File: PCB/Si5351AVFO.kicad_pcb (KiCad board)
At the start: 4 copper layers, 100 x 65 mm, 121 parts, among them J1 USB_C_Receptacle, J2 SMA CLK0, J3 SMA CLK1, J4 SMA CLK2, J5 UPDI, SW1 EC11E18244A5, SW2 BAND, SW3 STEP, SW4 MENU, U1 LP2985-3.3, U2 Si5351A-B-GT, U3 CP2102N-A02-GQFN24, U4 ATtiny3226-SU, U5 LP2985-3.3, X1 25MHz TCXO

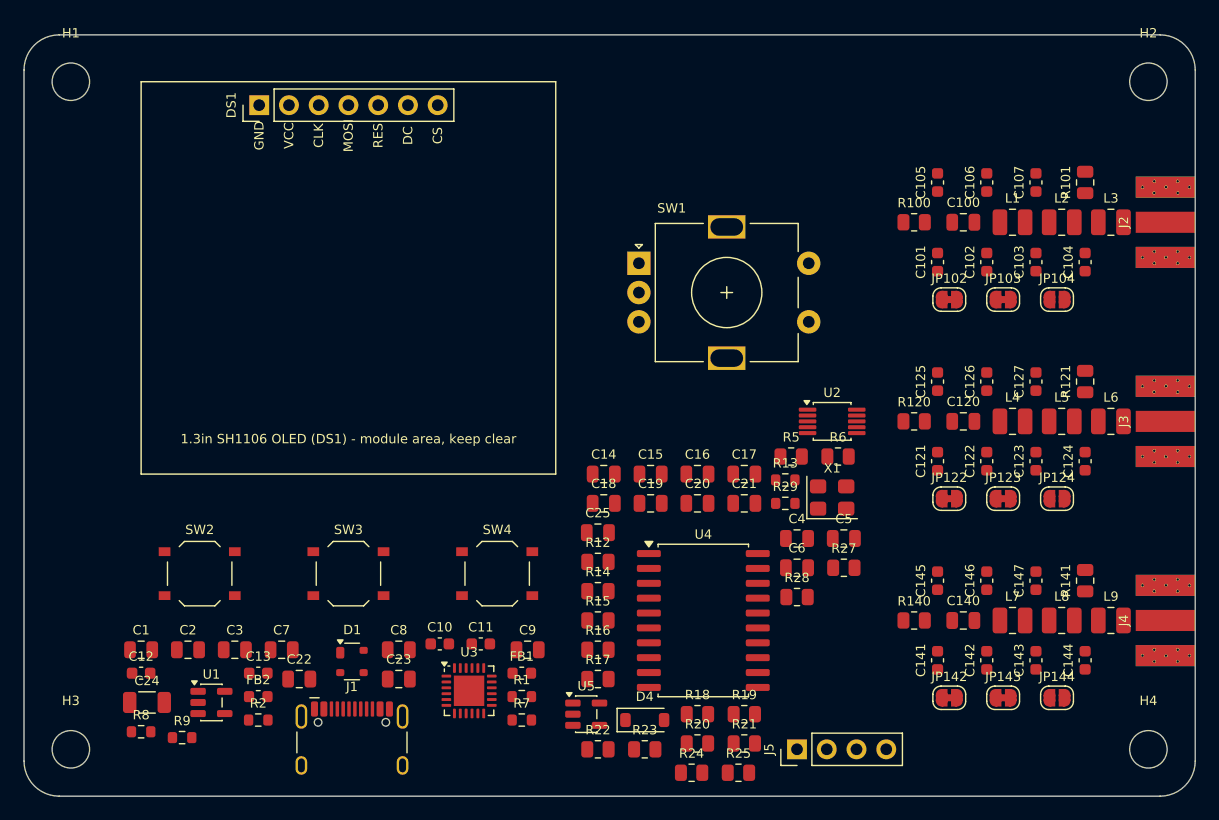
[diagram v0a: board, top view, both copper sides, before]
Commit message: Layout rev 2: USB-C + SMAs on top edge, RF block under SH1 fence, 11 mm tact switches, plated GND M3 holes, In1 cut under SMA centre pads, In1/In2 GND planes, Etherkit branding + Rev A on F.Cu; regen renders/outline/STEP
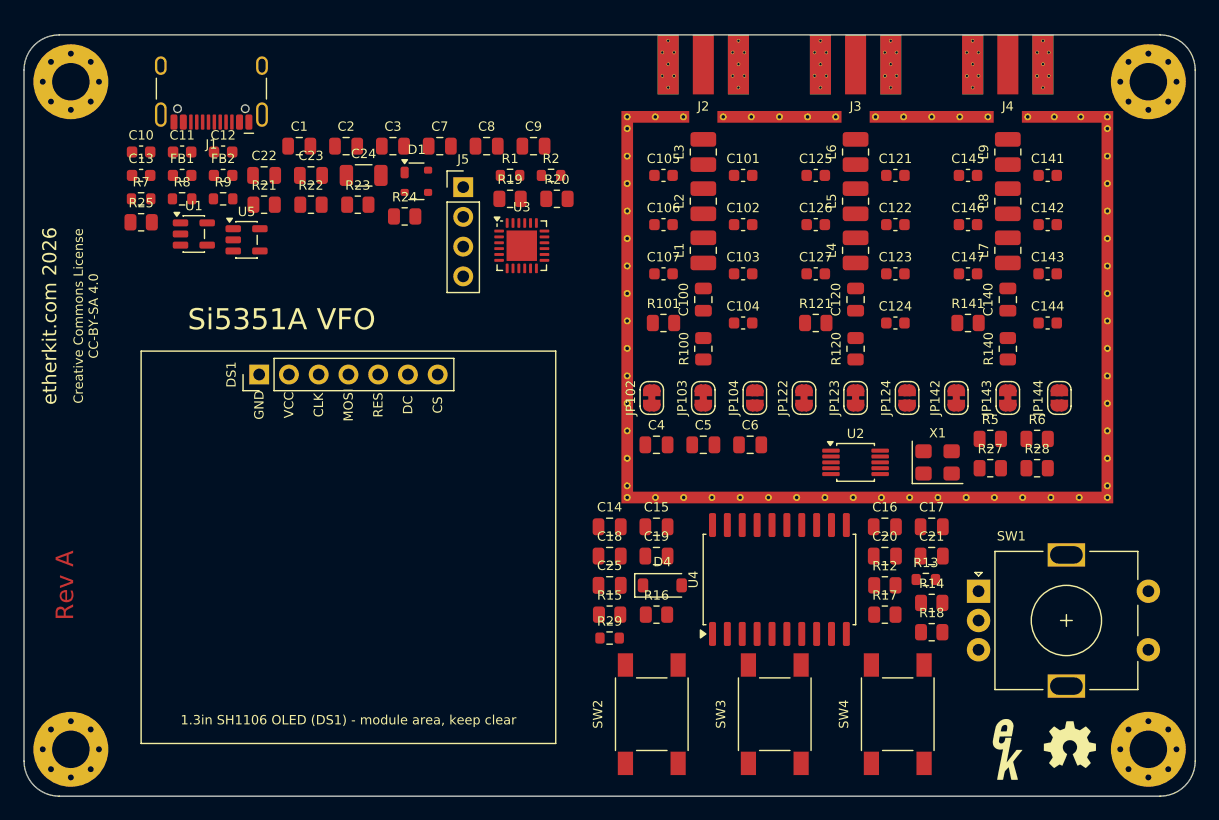
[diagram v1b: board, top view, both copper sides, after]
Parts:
- added LOGO1: Val**, EtherkitKicadLibrary:EtherkitLogoSmall, F.Cu at (184.0, 161.0)
- added LOGO2: Logo_Open_Hardware_Small, EtherkitKicadLibrary:OSHWLogo4mm, F.Cu at (189.3, 160.6)
- added SH1: RF_FENCE, EtherkitKicadLibrary:RF_Fence_42x33.5mm, F.Cu at (151.0, 106.5)
- H1, H2, H3, H4: footprint MountingHole:MountingHole_3.2mm_M3 -> MountingHole:MountingHole_3.2mm_M3_Pad_Via
- SW2, SW3, SW4: footprint Button_Switch_SMD:SW_Push_1P1T_XKB_TS-1187A -> EtherkitKicadLibrary:SW_Push_6x6mm_SMD_KH-6X6X11H-STM
- moved R25 69.4 mm to (110.0, 116.0)
- moved R21 61.6 mm to (120.5, 114.5)
- moved J1 58.8 mm to (116.0, 103.7), turned to 180 degrees
- moved J5 55.8 mm to (137.5, 113.0), turned to 0 degrees
- moved R7 55.1 mm to (110.0, 114.0)
- moved R24 53.4 mm to (132.5, 115.5)
- moved R2 52.8 mm to (145.0, 112.0)
- moved R22 52.6 mm to (124.5, 114.5)
- moved R23 52.6 mm to (128.5, 114.5)
- moved J4 52.5 mm to (184.0, 100.0), turned to 180 degrees
- moved FB1 51.5 mm to (113.5, 112.0)
- moved U5 49.8 mm to (119.0, 117.5)
- moved C10 49.1 mm to (110.0, 110.0)
- moved C11 49.1 mm to (113.5, 110.0)
- moved C24 48.7 mm to (129.0, 112.0)
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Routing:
- added copper zone on In1.Cu, net GND
- added copper zone on In2.Cu, net GND
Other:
- board text added: "Creative Commons License CC-BY-SA 4.0"
- board text added: "Rev A"
- board text added: "Si5351A VFO"
- board text added: "etherkit.com 2026"
- board text removed: "Si5351A VFO Rev A NT7S / Etherkit"

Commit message: Layout: buttons back in a row under OLED (OLED moved up), Si5351 decoupling at U2/X1 pins, power/USB tidied (LDO rows Cin-U-Cout-FB), CLK0-2 labels, horizontal front branding, back-silk book line, silkscreen overlaps cleared; regen renders/outline/STEP
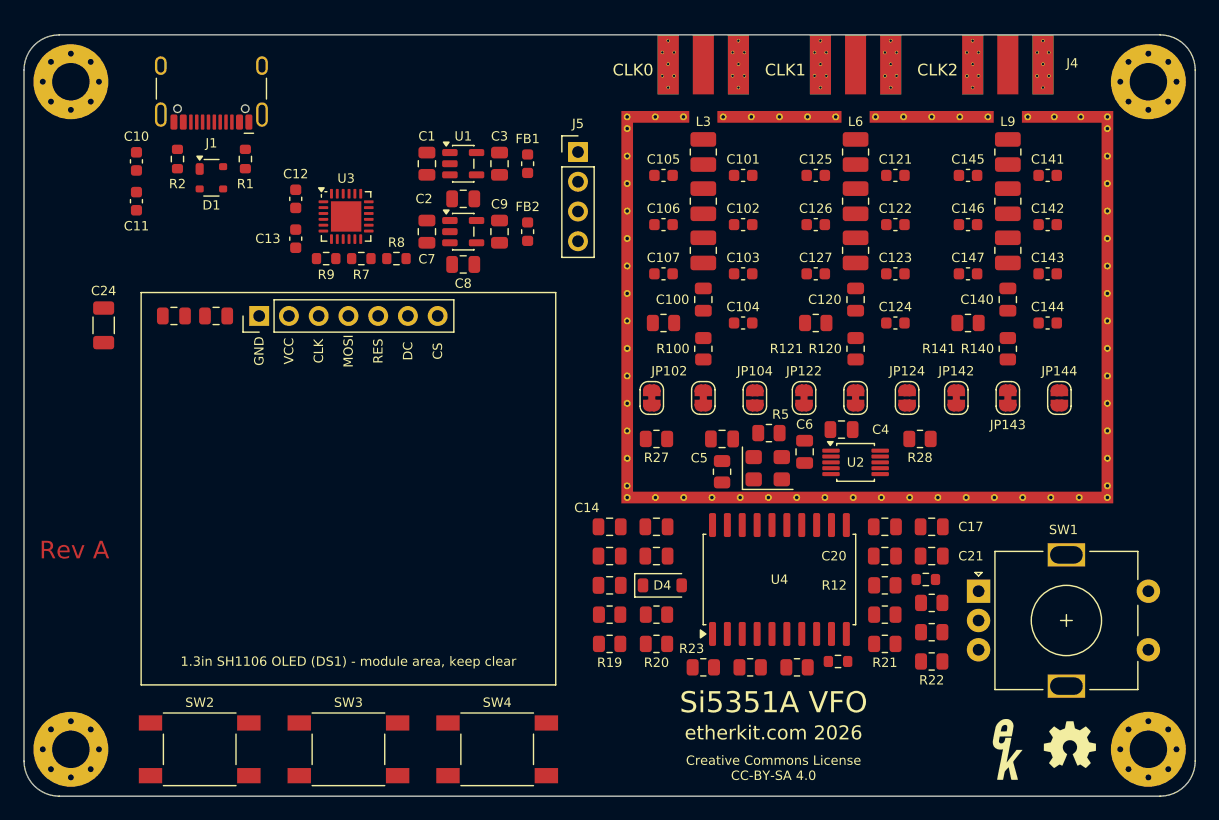
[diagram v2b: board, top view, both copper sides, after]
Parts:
- moved R25 67.7 mm to (166.0, 154.0)
- moved R22 65.8 mm to (177.5, 153.5)
- moved R21 64.9 mm to (173.5, 152.0)
- moved R23 49.3 mm to (158.0, 154.0)
- moved R24 48.5 mm to (162.0, 154.0)
- moved R19 38.9 mm to (150.0, 152.0)
- moved R20 38.9 mm to (154.0, 152.0)
- moved SW2 38.7 mm to (115.0, 161.0), turned to 0 degrees
- moved SW3 36.5 mm to (127.7, 161.0), turned to 0 degrees
- moved SW4 34.3 mm to (140.4, 161.0), turned to 0 degrees
- moved R2 31.9 mm to (113.1, 110.6), turned to 90 degrees
- moved FB1 29.5 mm to (143.0, 111.0), turned to 90 degrees
- moved R27 28.6 mm to (154.0, 134.5)
- moved R6 27.0 mm to (159.6, 137.3), turned to 90 degrees
- moved FB2 26.4 mm to (143.0, 116.8), turned to 90 degrees
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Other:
- board text added: "CLK0"
- board text added: "CLK1"
- board text added: "CLK2"
- board text added: "Si5351 Field Manual, Chapter 6"

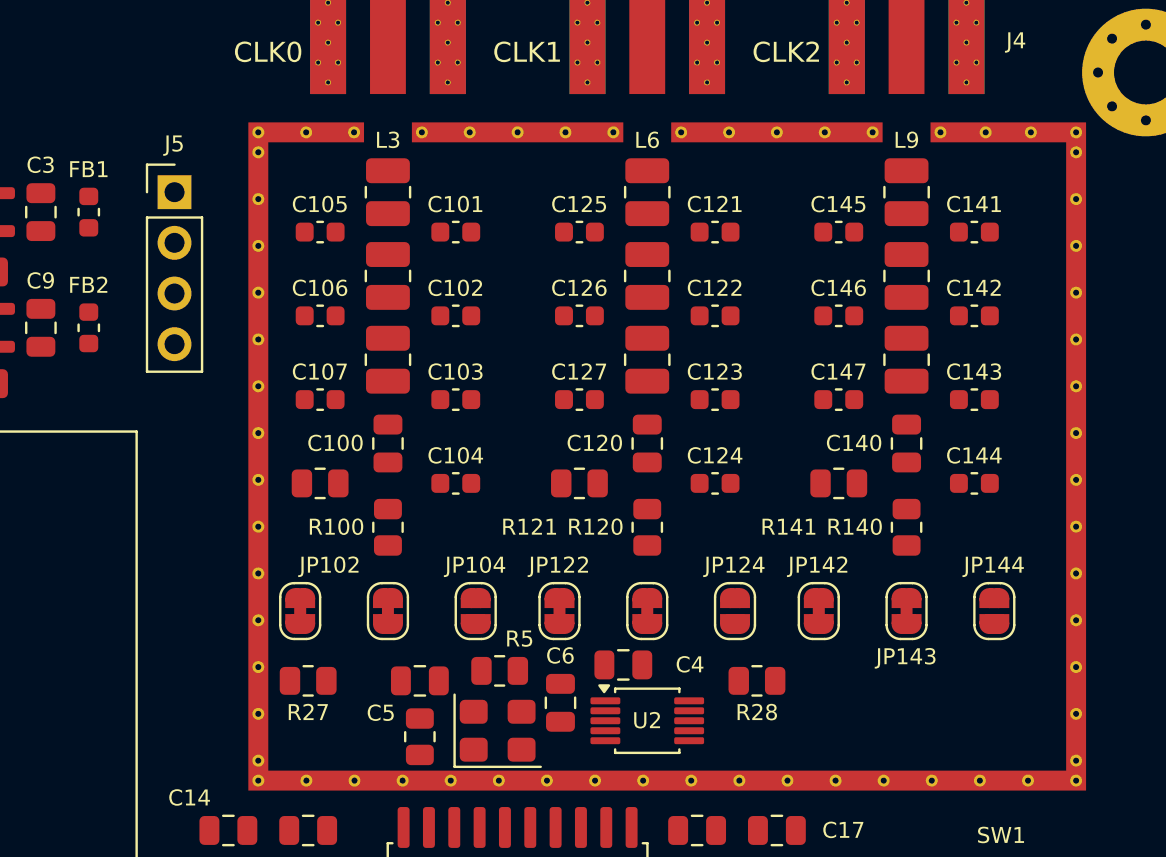
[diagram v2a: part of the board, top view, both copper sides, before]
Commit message: Layout: straight-line LPF per channel (in-select -> 3-section Cauer ladder -> out-select -> SMA), bypass jumper at input end behind GND via fence; J5 UPDI title + pin labels
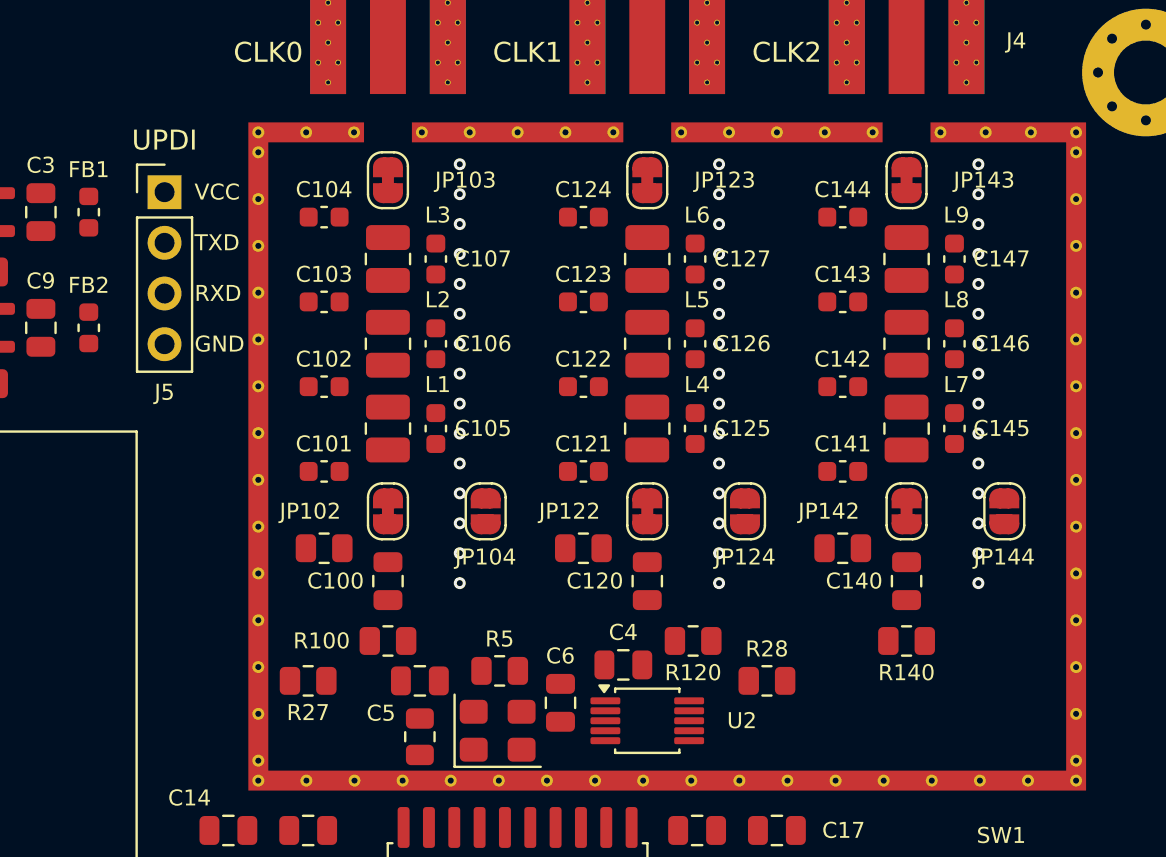
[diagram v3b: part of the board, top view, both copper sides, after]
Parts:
- moved JP103 21.6 mm to (158.0, 109.4)
- moved JP123 21.6 mm to (171.0, 109.4)
- moved JP143 21.6 mm to (184.0, 109.4)
- moved C104 14.9 mm to (154.8, 111.2)
- moved C124 14.9 mm to (167.8, 111.2)
- moved C144 14.9 mm to (180.8, 111.2)
- moved C101 13.7 mm to (154.8, 124.0)
- moved C121 13.7 mm to (167.8, 124.0)
- moved C141 13.7 mm to (180.8, 124.0)
- moved C105 11.4 mm to (160.4, 121.8), turned to 90 degrees
- moved C125 11.4 mm to (173.4, 121.8), turned to 90 degrees
- moved C145 11.4 mm to (186.4, 121.8), turned to 90 degrees
- moved C107 9.13 mm to (160.4, 113.3), turned to 90 degrees
- moved C127 9.13 mm to (173.4, 113.3), turned to 90 degrees
- moved C147 9.13 mm to (186.4, 113.3), turned to 90 degrees
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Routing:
- net GND: vias 0 -> 45
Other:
- board text added: "RXD"
- board text added: "TXD"
- board text added: "UPDI"

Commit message: Layout: SMA-end bypass jumpers JP105/JP125/JP145 at top of each guarded bypass lane; netlist sync
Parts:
- added JP105: NO, Jumper:SolderJumper-2_P1.3mm_Open_RoundedPad1.0x1.5mm, F.Cu at (162.9, 109.4)
- added JP125: NO, Jumper:SolderJumper-2_P1.3mm_Open_RoundedPad1.0x1.5mm, F.Cu at (175.9, 109.4)
- added JP145: NO, Jumper:SolderJumper-2_P1.3mm_Open_RoundedPad1.0x1.5mm, F.Cu at (188.9, 109.4)
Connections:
- JP104 pad 2: Net-(J2-In) -> /Synth and RF outputs/CLK0_BYP
- JP124 pad 2: Net-(J3-In) -> /Synth and RF outputs/CLK1_BYP
- JP144 pad 2: Net-(J4-In) -> /Synth and RF outputs/CLK2_BYP

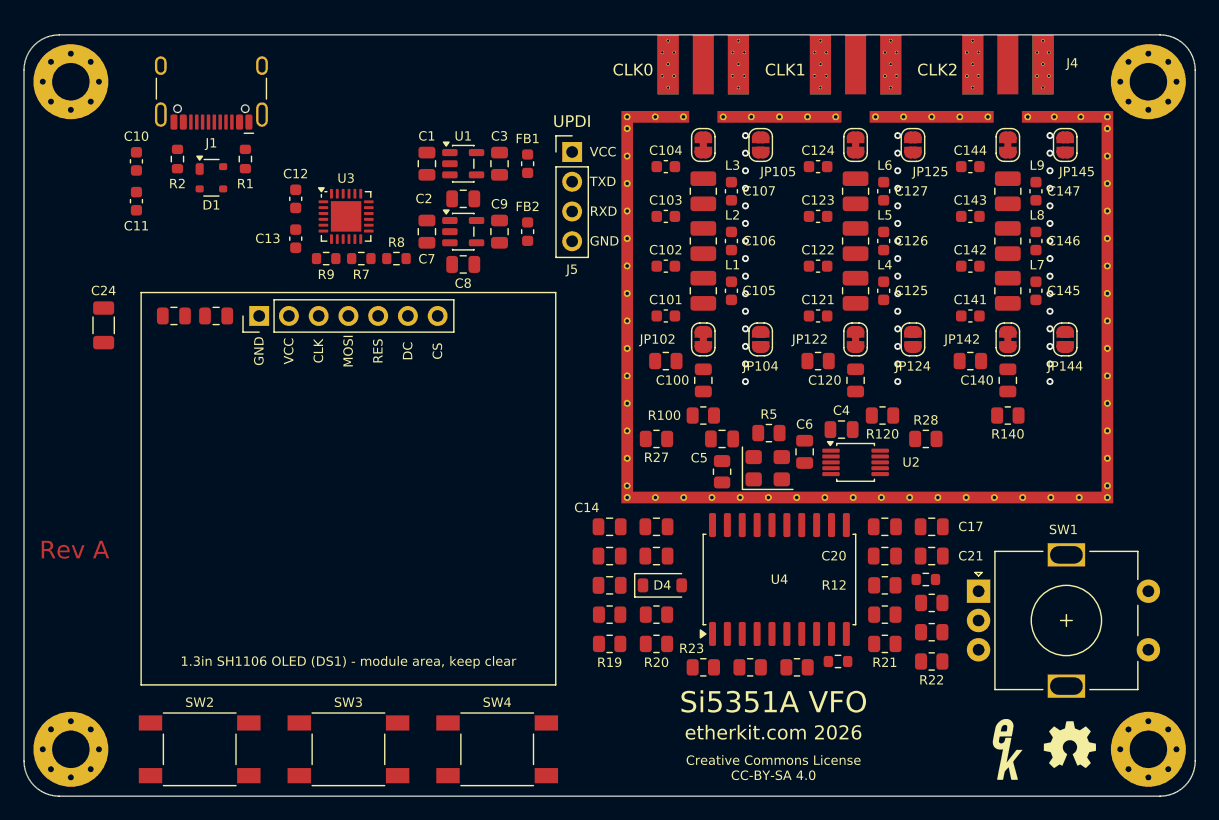
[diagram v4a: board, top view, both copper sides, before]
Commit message: Route RF: CLK0-2 0.35 mm CPWG (gap 0.20) through series R, DC block, select jumpers, Cauer LPF, bypass lane to SMAs; GND vias at all SMD GND pads; RF stitching; F/B GND pours
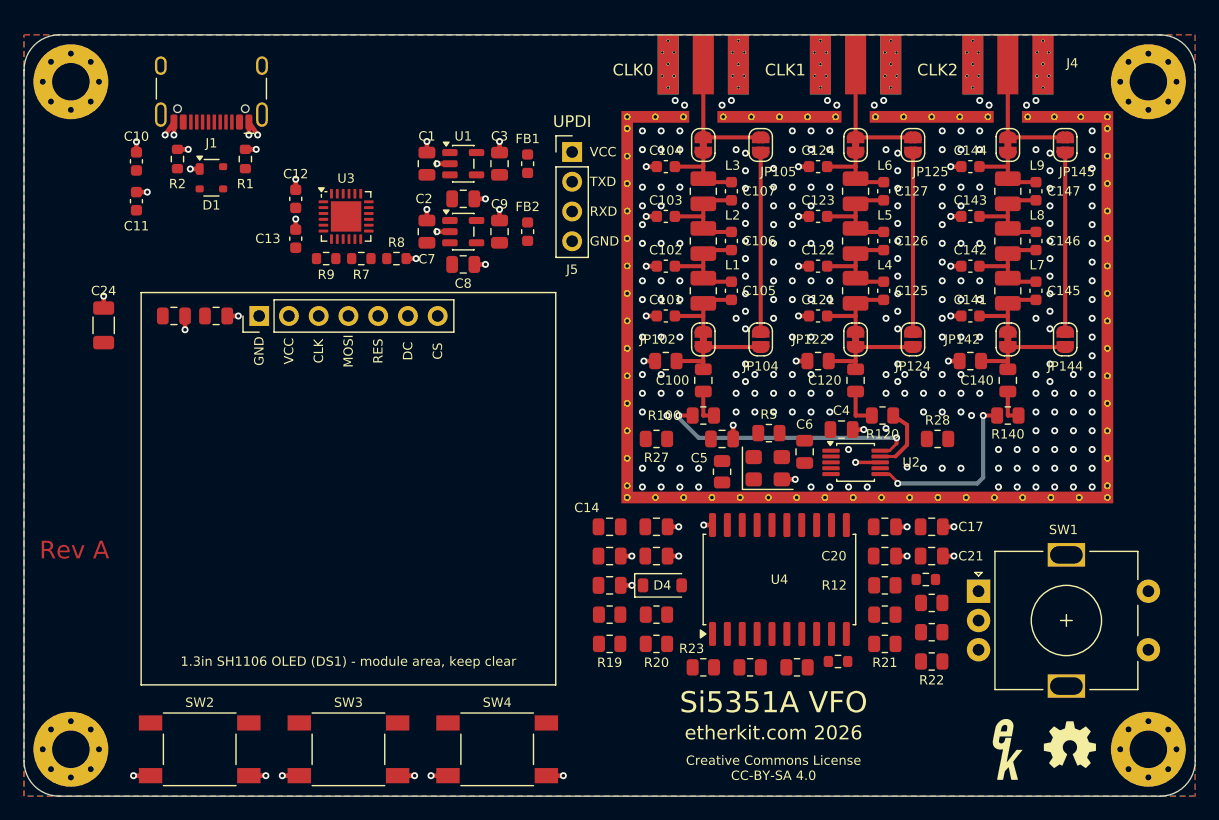
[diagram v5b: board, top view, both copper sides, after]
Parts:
- moved R28 1.00 mm to (178.0, 134.5)
- turned C101 to 180 degrees
- turned C102 to 180 degrees
- turned C103 to 180 degrees
- turned C104 to 180 degrees
- turned C121 to 180 degrees
- turned C122 to 180 degrees
- turned C123 to 180 degrees
- turned C124 to 180 degrees
- turned C141 to 180 degrees
- turned C142 to 180 degrees
- turned C143 to 180 degrees
- turned C144 to 180 degrees
- turned R101 to 180 degrees
- turned R120 to 180 degrees
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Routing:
- net GND: track 0.00 -> 59.2 mm, vias 45 -> 300
- net /Synth and RF outputs/CLK0: track 0.00 -> 22.8 mm, vias 0 -> 2
- net /Synth and RF outputs/CLK2: track 0.00 -> 15.9 mm, vias 0 -> 2
- net /Synth and RF outputs/CLK2_BYP: track 0.00 -> 15.3 mm
- net /Synth and RF outputs/CLK1_BYP: track 0.00 -> 15.3 mm
- net /Synth and RF outputs/CLK0_BYP: track 0.00 -> 15.3 mm
- net Net-(J4-In): track 0.00 -> 11.1 mm
- net Net-(J3-In): track 0.00 -> 11.1 mm
- net Net-(J2-In): track 0.00 -> 11.1 mm
- net Net-(C143-Pad1): track 0.00 -> 9.33 mm
- net Net-(C142-Pad1): track 0.00 -> 9.33 mm
- net Net-(C123-Pad1): track 0.00 -> 9.33 mm
- net Net-(C122-Pad1): track 0.00 -> 9.33 mm
- net Net-(C103-Pad1): track 0.00 -> 9.33 mm
- net Net-(C102-Pad1): track 0.00 -> 9.33 mm
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- added copper zone on B.Cu, net GND
- added copper zone on F.Cu, net GND
